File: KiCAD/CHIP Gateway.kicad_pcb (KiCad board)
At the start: 2 copper layers, 40.6 x 60.3 mm, 9 parts, among them P1 CONN_01X02, P2 CONN_01X04, P3 CONN_01X04, U1 CHIP_Shield, U2 RFM69, U3 DS3231

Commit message: Ready for ordering
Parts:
- added P4: CONN_01X05, Connectors_JST:JST_XH_S05B-XH-A_05x2.50mm_Angled, F.Cu at (151.1, 101.2)
- added P5: CONN_01X05, Connectors_JST:JST_XH_S05B-XH-A_05x2.50mm_Angled, F.Cu at (135.9, 101.2)
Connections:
- U1 pad 17: (no net) -> TX2
- U1 pad 20: (no net) -> RX2
- U1 pad 3: (no net) -> +5V
- U1 pad 43: (no net) -> TX1
- U1 pad 45: (no net) -> RX1
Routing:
- net +5V: track 0.00 -> 65.9 mm
- net TX1: track 0.00 -> 52.8 mm, vias 0 -> 2
- net RX1: track 0.00 -> 49.9 mm, vias 0 -> 1
- net TX2: track 0.00 -> 36.2 mm, vias 0 -> 1
- net RX2: track 0.00 -> 33.9 mm, vias 0 -> 1
- net +3V3: track 31.7 -> 36.9 mm, vias 2 -> 3
- net I2C1-SCK: track 54.3 -> 52.8 mm
- net Net-(BT1-Pad1): track 44.6 -> 45.4 mm
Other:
- net class HighPwr added: clearance 0.2032, trace_width 0.508, via_dia 0.6, via_drill 0.4
- board text added: "3V3"
- board text added: "5V"
- board text added: "Gnd"
- board text added: "RX"
- board text added: "SCK"
- board text added: "SDA"
- board text added: "TX"
- board text added: "https://github.com/tht/chip-rfm-gateway"

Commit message: Ready for ordering
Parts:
- turned BT1 to 0 degrees
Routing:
- net GND: track 8.89 -> 71.0 mm, vias 1 -> 15
- added copper zone on B.Cu, net GND
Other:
- board text added: "UART1"
- board text added: "UART2"

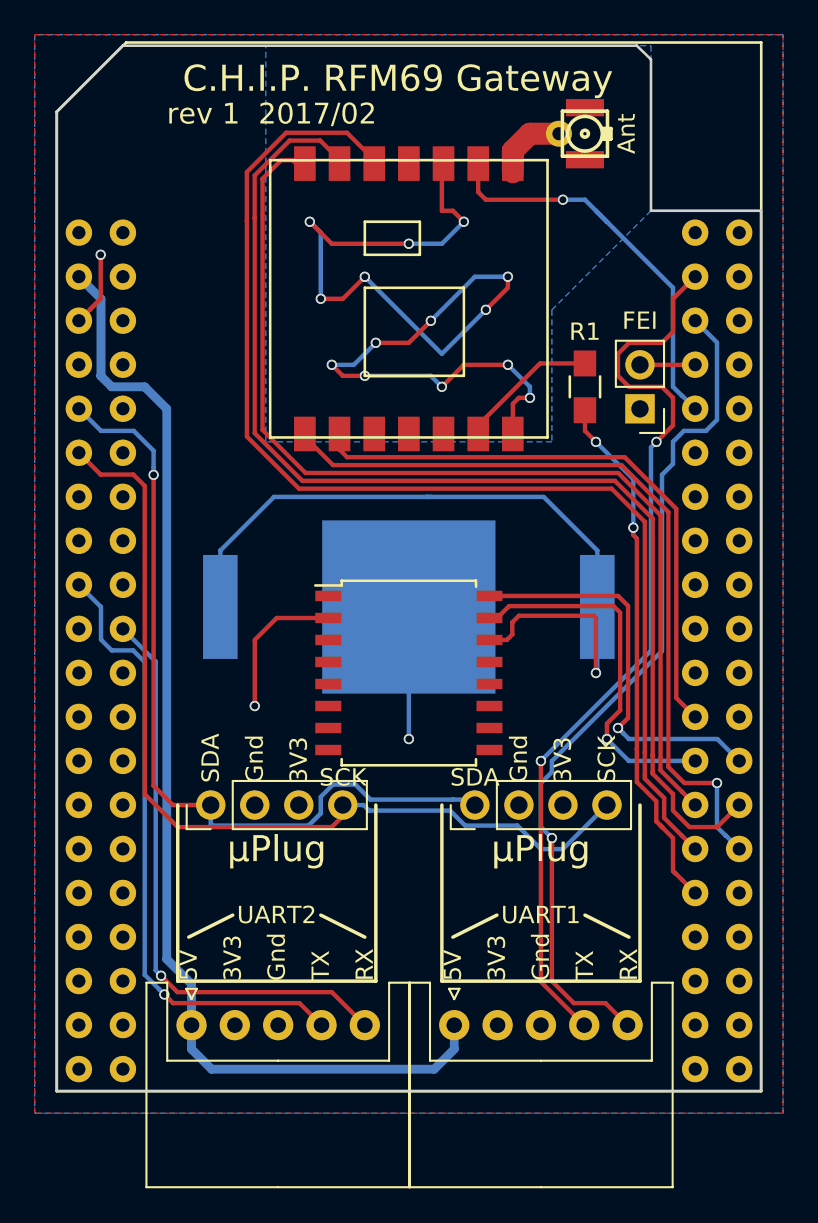
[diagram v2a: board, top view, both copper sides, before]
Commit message: Connected DIO1
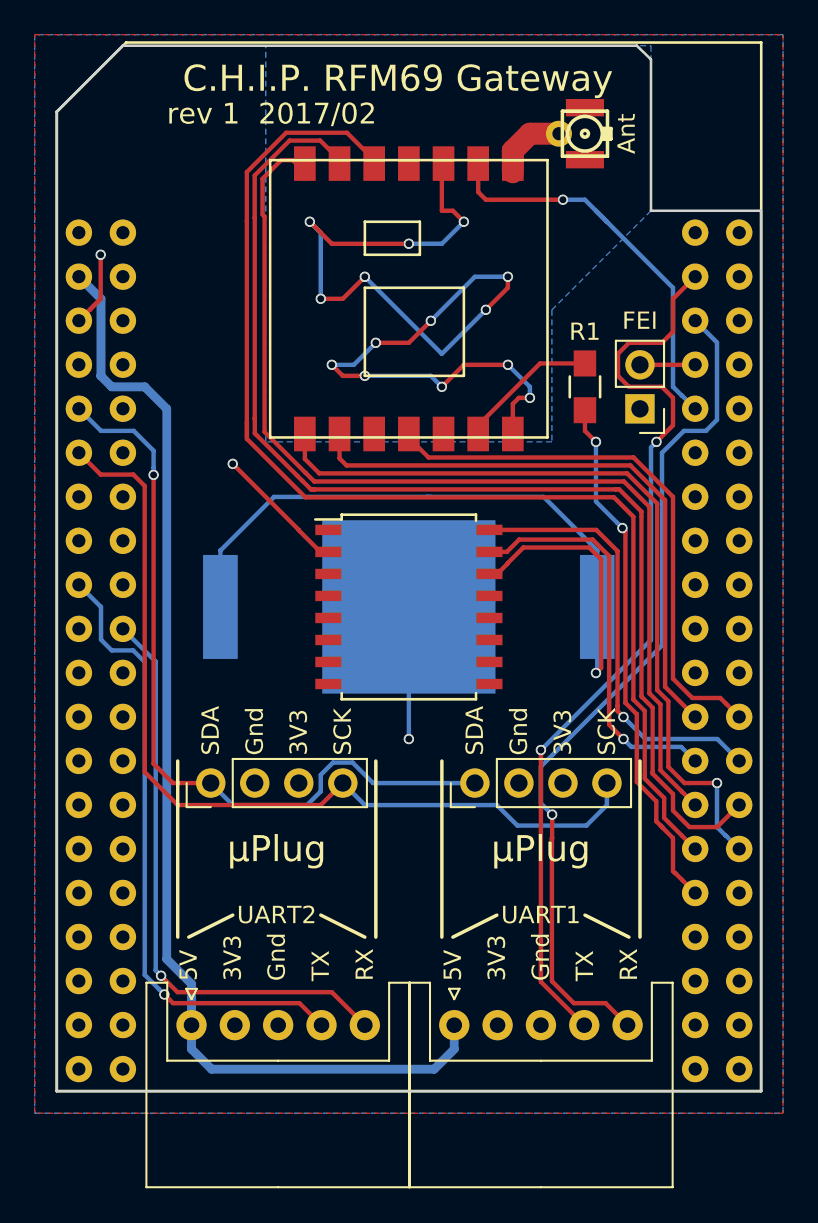
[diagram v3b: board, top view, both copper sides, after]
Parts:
- moved U3 3.81 mm to (148.5, 77.1)
- moved P2 1.27 mm to (152.3, 87.2)
- moved P3 1.27 mm to (137.1, 87.2)
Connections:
- U1 pad 64: (no net) -> RFM_INT2
- U2 pad 11: (no net) -> RFM_INT2
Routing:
- net RFM_INT2: track 0.00 -> 32.6 mm
- net Net-(BT1-Pad1): track 45.4 -> 49.1 mm
- net I2C2-SCK: track 23.3 -> 25.3 mm
- net I2C2-SDA: track 21.2 -> 23.2 mm
- net I2C1-SDA: track 46.8 -> 45.0 mm
- net I2C1-SCK: track 52.8 -> 51.9 mm
- net +3V3: track 36.9 -> 35.9 mm
- net MOSI: track 70.0 -> 70.7 mm
- net MISO: track 46.9 -> 47.5 mm

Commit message: Rev 1 as ordered
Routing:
- net GND: track 71.0 -> 82.9 mm, vias 15 -> 16
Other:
- board text added: "rev 1 2017/03"
- board text removed: "rev 1 2017/02"
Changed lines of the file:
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@@
     (links 58)
     (no_connects 0)
-    (area 128.094999 44.604999 168.885001 105.085001)
+    (area 126.9 44.05 170.080001 112.629)
     (thickness 1.6)
     (drawings 43)
-    (tracks 358)
+    (tracks 359)
     (zones 0)
     (modules 11)
@@
     (last_trace_width 0.254)
     (trace_clearance 0.2032)
-    (zone_clearance 0.3048)
+    (zone_clearance 0.254)
     (zone_45_only no)
     (trace_min 0.2)
@@
     (effects (font (size 1 1) (thickness 0.15)))
   )
-  (gr_text "rev 1  2017/02" (at 134.52 48.622) (layer F.SilkS)
+  (gr_text "rev 1  2017/03" (at 134.52 48.622) (layer F.SilkS)
     (effects (font (size 1.2 1.2) (thickness 0.2)) (justify left))
   )
@@
   (gr_line (start 168.81 54.21) (end 162.46 54.21) (layer Edge.Cuts) (width 0.15))
   (gr_line (start 128.17 105.01) (end 168.81 105.01) (layer Edge.Cuts) (width 0.15))
+  (via (at 166.27 69.45) (size 0.6) (drill 0.4) (layers F.Cu B.Cu) (net 1))
+  (segment (start 166.27 79.5925) (end 166.27 69.45) (width 0.254) (layer B.Cu) (net 1))
+  (segment (start 167.5511 80.8736) (end 166.27 79.5925) (width 0.254) (layer B.Cu) (net 1))
   (segment (start 150.395 54.21) (end 150.395 52.085) (width 0.254) (layer F.Cu) (net 1))
   (segment (start 150.395 52.085) (end 150.49 51.99) (width 0.254) (layer F.Cu) (net 1))
@@
   (segment (start 161.825 63.1) (end 165.0047 63.1) (width 0.254) (layer F.Cu) (net 3))
   (segment (start 165.0047 63.1) (end 165.0111 63.0936) (width 0.254) (layer F.Cu) (net 3))
+  (segment (start 133.76279 69.45) (end 133.76279 67.42279) (width 0.254) (layer B.Cu) (net 4))
+  (segment (start 133.76279 67.42279) (end 133.25 66.91) (width 0.254) (layer B.Cu) (net 4))
+  (segment (start 129.4511 65.6336) (end 130.7275 66.91) (width 0.254) (layer B.Cu) (net 4))
+  (segment (start 130.7275 66.91) (end 133.25 66.91) (width 0.254) (layer B.Cu) (net 4))
   (segment (start 133.76279 86.117212) (end 133.76279 69.45) (width 0.254) (layer F.Cu) (net 4))
   (segment (start 137.06 87.23) (end 138.33 88.5) (width 0.254) (layer B.Cu) (net 4))
@@
   (segment (start 134.875578 87.23) (end 137.06 87.23) (width 0.254) (layer F.Cu) (net 4))
   (segment (start 133.76279 86.117212) (end 134.875578 87.23) (width 0.254) (layer F.Cu) (net 4))
-  (segment (start 133.76279 69.025736) (end 133.76279 69.45) (width 0.254) (layer B.Cu) (net 4))
-  (segment (start 132.615 66.91) (end 133.76279 68.05779) (width 0.254) (layer B.Cu) (net 4))
-  (segment (start 130.7275 66.91) (end 132.615 66.91) (width 0.254) (layer B.Cu) (net 4))
-  (segment (start 129.4511 65.6336) (end 130.7275 66.91) (width 0.254) (layer B.Cu) (net 4))
-  (segment (start 133.76279 68.05779) (end 133.76279 69.025736) (width 0.254) (layer B.Cu) (net 4))
   (via (at 133.76279 69.45) (size 0.6) (drill 0.4) (layers F.Cu B.Cu) (net 4))
   (segment (start 142.14 72.625) (end 138.33 68.815) (width 0.254) (layer F.Cu) (net 5))
@@
   (segment (start 163.73 64.37) (end 164.231601 64.871601) (width 0.254) (layer B.Cu) (net 5))
   (segment (start 164.249101 64.871601) (end 165.0111 65.6336) (width 0.254) (layer B.Cu) (net 5))
-  (segment (start 159.92 88.5) (end 159.92 87.23) (width 0.254) (layer B.Cu) (net 6))
-  (segment (start 145.95 88.5) (end 153.57 88.5) (width 0.254) (layer B.Cu) (net 6))
-  (segment (start 144.68 87.23) (end 145.95 88.5) (width 0.254) (layer B.Cu) (net 6))
-  (segment (start 153.57 88.5) (end 154.750201 89.680201) (width 0.254) (layer B.Cu) (net 6))
-  (segment (start 154.750201 89.680201) (end 158.739799 89.680201) (width 0.254) (layer B.Cu) (net 6))
-  (segment (start 158.739799 89.680201) (end 159.92 88.5) (width 0.254) (layer B.Cu) (net 6))
+  (segment (start 159.92 87.23) (end 159.92 88.5) (width 0.254) (layer B.Cu) (net 6))
+  (segment (start 159.92 88.5) (end 158.739799 89.680201) (width 0.254) (layer B.Cu) (net 6))
+  (segment (start 158.739799 89.680201) (end 147.130201 89.680201) (width 0.254) (layer B.Cu) (net 6))
+  (segment (start 147.130201 89.680201) (end 145.315 87.865) (width 0.254) (layer B.Cu) (net 6))
+  (segment (start 145.315 87.865) (end 144.68 87.23) (width 0.254) (layer B.Cu) (net 6))
   (segment (start 135.155 88.5) (end 143.41 88.5) (width 0.254) (layer F.Cu) (net 6))
   (segment (start 144.68 87.23) (end 143.41 88.5) (width 0.254) (layer F.Cu) (net 6))
@@
   (segment (start 156.11 98.7) (end 158.61 101.2) (width 0.254) (layer F.Cu) (net 18))
   (via (at 156.11 85.325) (size 0.6) (drill 0.4) (layers F.Cu B.Cu) (net 18))
+  (segment (start 156.11 86.2775) (end 156.11 88.40237) (width 0.254) (layer B.Cu) (net 19))
   (segment (start 156.757621 89.049991) (end 156.11 88.40237) (width 0.254) (layer B.Cu) (net 19))
-  (segment (start 156.11 88.40237) (end 156.11 86.2775) (width 0.254) (layer B.Cu) (net 19))
   (segment (start 156.11 86.2775) (end 163.095 79.2925) (width 0.254) (layer B.Cu) (net 19))
   (segment (start 163.095 68.18) (end 164.365 66.91) (width 0.254) (layer B.Cu) (net 19))
@@
   (segment (start 130.7275 63.7175) (end 130.71 63.735) (width 0.508) (layer B.Cu) (net 21))
   (segment (start 130.71 63.735) (end 131.345 64.37) (width 0.508) (layer B.Cu) (net 21))
-  (segment (start 131.345 64.37) (end 133.25 64.37) (width 0.508) (layer B.Cu) (net 21))
-  (segment (start 133.25 64.37) (end 134.52 65.64) (width 0.508) (layer B.Cu) (net 21))
-  (segment (start 134.52 65.64) (end 134.52 97.39) (width 0.508) (layer B.Cu) (net 21))
+  (segment (start 131.345 64.37) (end 132.615 64.37) (width 0.508) (layer B.Cu) (net 21))
+  (segment (start 132.615 64.37) (end 134.52 66.275) (width 0.508) (layer B.Cu) (net 21))
+  (segment (start 134.52 66.275) (end 134.52 97.39) (width 0.508) (layer B.Cu) (net 21))
   (segment (start 134.52 97.39) (end 135.95 98.82) (width 0.508) (layer B.Cu) (net 21))
   (segment (start 135.95 98.82) (end 135.95 101.2) (width 0.508) (layer B.Cu) (net 21))
@@
   (segment (start 166.789101 82.651601) (end 167.5511 83.4136) (width 0.254) (layer F.Cu) (net 22))
   (zone (net 1) (net_name GND) (layer F.Cu) (hatch edge 0.508)
-    (connect_pads (clearance 0.3048))
+    (connect_pads (clearance 0.254))
     (min_thickness 0.254)
     (fill yes (arc_segments 16) (thermal_gap 0.381) (thermal_bridge_width 0.508) (smoothing chamfer))
@@
   )
   (zone (net 5) (net_name +3V3) (layer B.Cu) (hatch edge 0.508)
-    (connect_pads (clearance 0.3048))
+    (connect_pads (clearance 0.254))
     (min_thickness 0.254)
     (fill yes (arc_segments 16) (thermal_gap 0.381) (thermal_bridge_width 0.508) (smoothing chamfer))
